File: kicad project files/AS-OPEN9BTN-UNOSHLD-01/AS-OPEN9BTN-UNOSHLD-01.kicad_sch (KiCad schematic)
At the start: 11 parts, among them J1 Conn_01x04, SW1 SW_Push, SW2 SW_Push, SW3 SW_Push, SW4 SW_Push, SW5 SW_Push, SW6 SW_Push, SW7 SW_Push, SW8 SW_Push, SW9 SW_Push

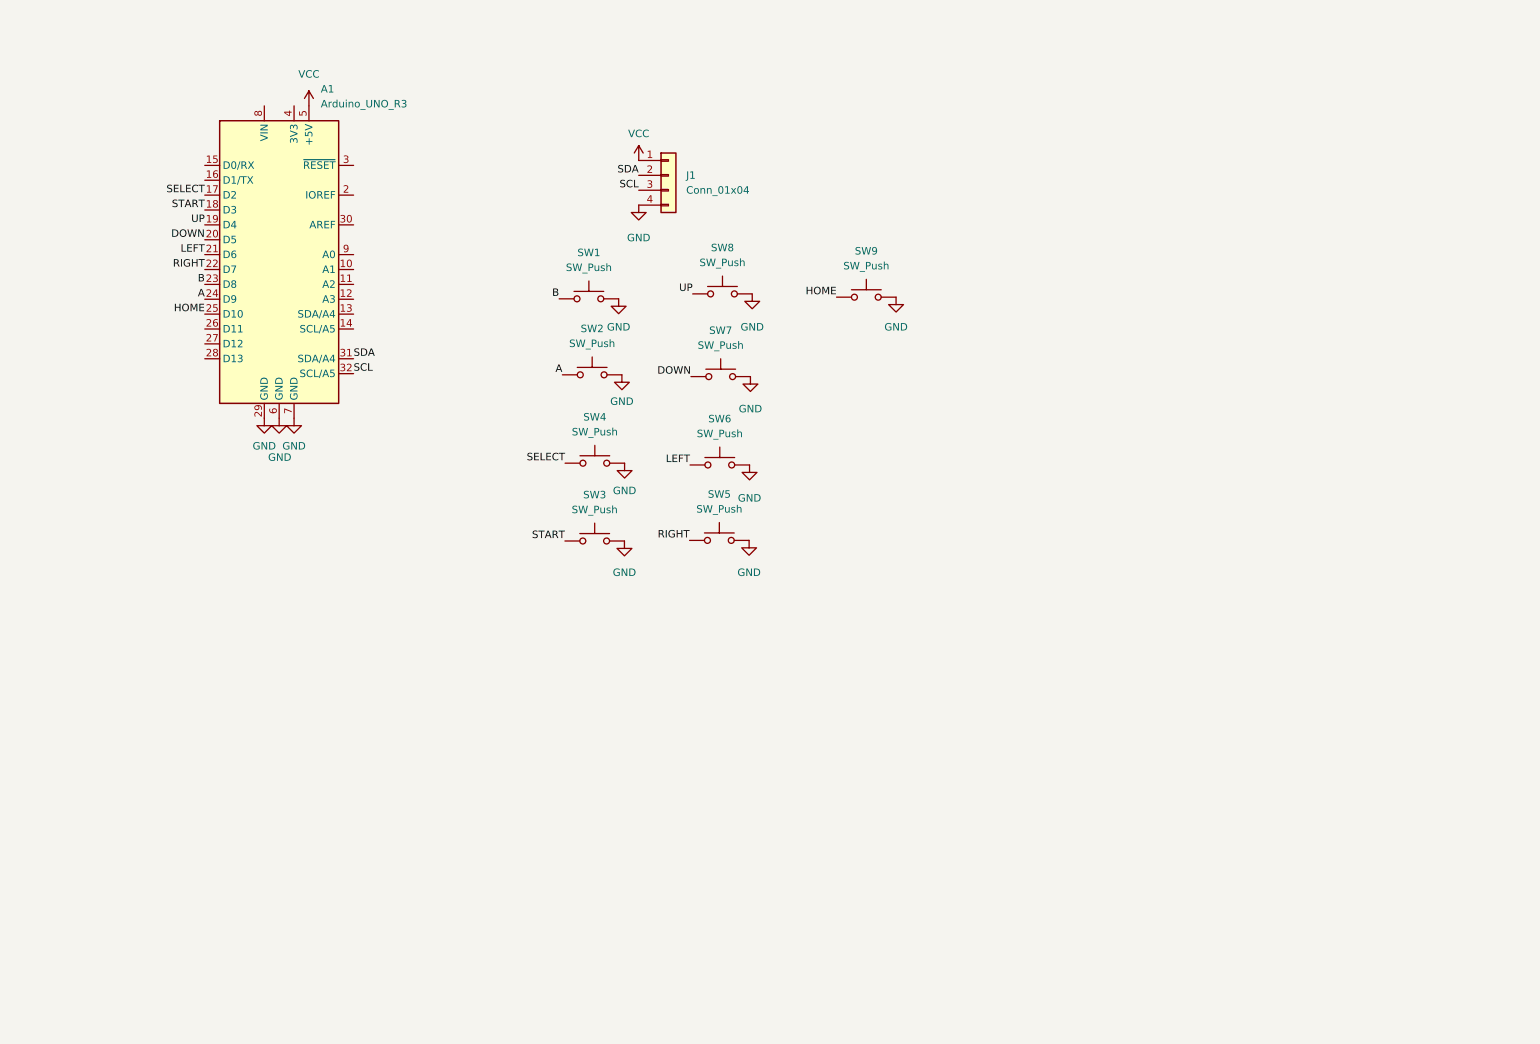
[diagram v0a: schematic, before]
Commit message: First step to voltage convertion
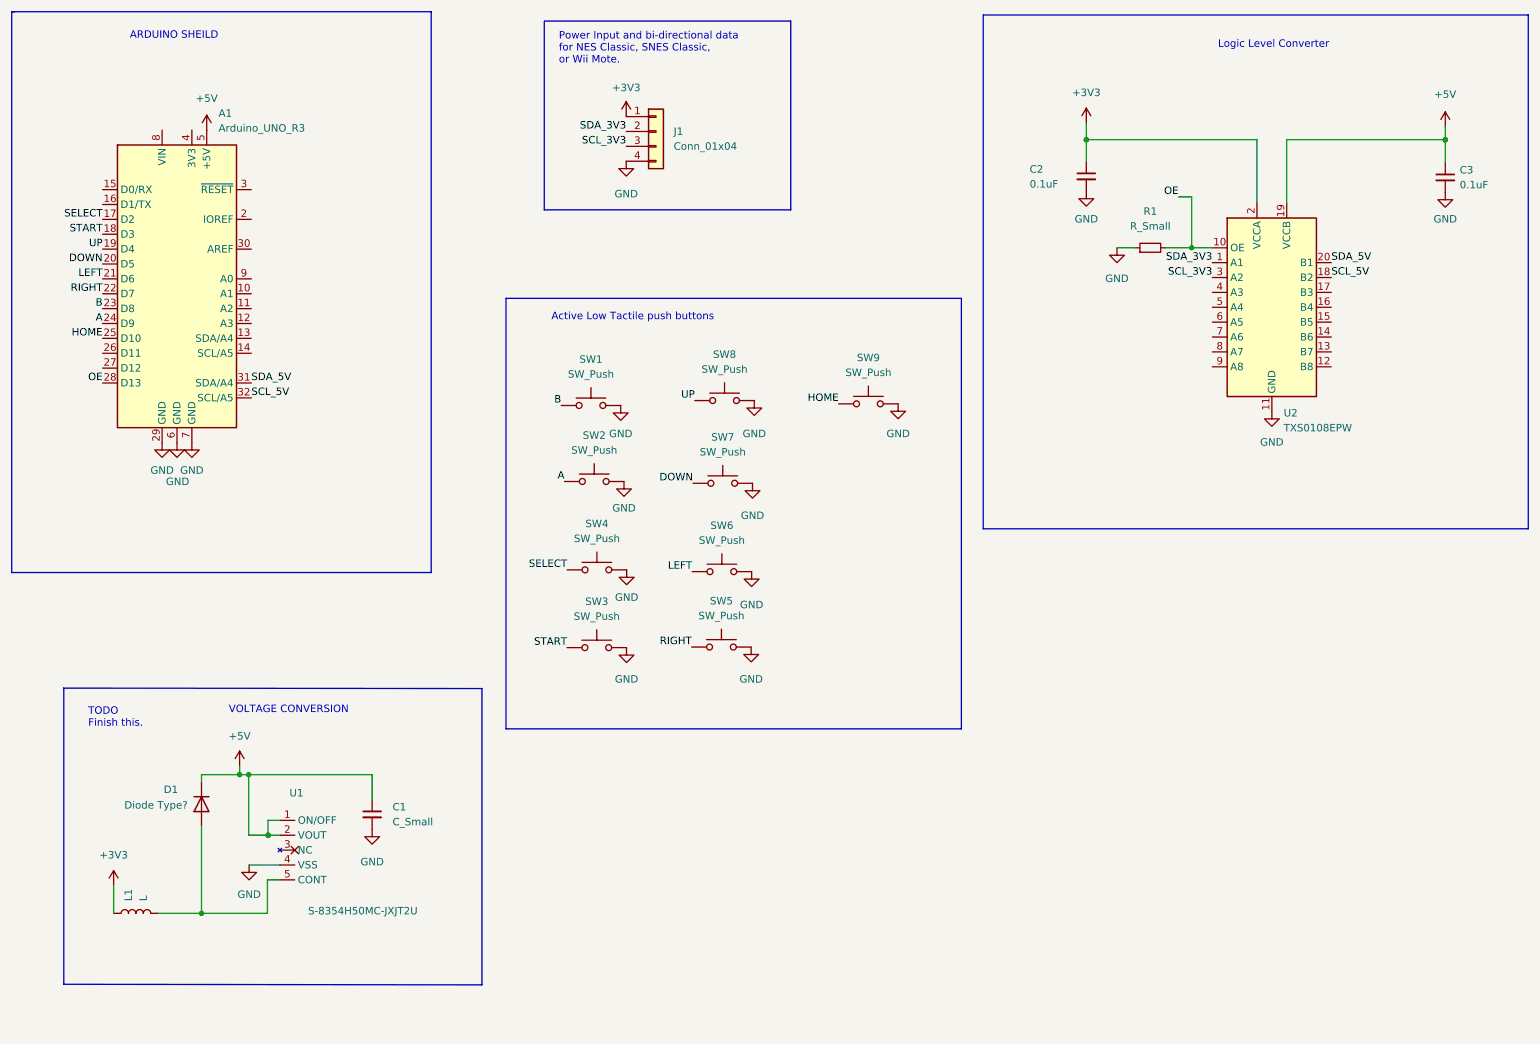
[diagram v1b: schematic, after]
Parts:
- added C1: C_Small, symbol Device:C_Small
- added C2, C3: 0.1uF, symbol Device:C_Small
- added D1: Diode Type?, Diode_THT:D_DO-41_SOD81_P10.16mm_Horizontal, symbol Diode:1N4001
- added L1: L, symbol Device:L
- added R1: R_Small, symbol Device:R_Small
- added U1: S-8354H50MC-JXJT2U, Package_TO_SOT_SMD:SOT-23-5_HandSoldering, symbol New_Library:S-8354H50MC-JXJT2U
- added U2: TXS0108EPW, Package_SO:TSSOP-20_4.4x6.5mm_P0.65mm, symbol Logic_LevelTranslator:TXS0108EPW
- J1: footprint (none) -> Connector_JST:JST_XH_B4B-XH-A_1x04_P2.50mm_Vertical
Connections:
- net GND: now also C1.2, C2.2, C3.2, R1.1, U1.4 (VSS), U2.11 (GND)
- net OE: now reaches A1.28 (D13)
- net OE: now also R1.2, U2.10 (OE)
- net SCL renamed SCL_3V3
- net SCL_3V3: now also U2.3 (A2); no longer A1.32 (SCL/A5)
- net SDA renamed SDA_3V3
- net SDA_3V3: now also U2.1 (A1); no longer A1.31 (SDA/A4)
- net VCC renamed +3V3
- net +3V3: now also C2.1, L1.1, U2.2 (VCCA); no longer A1.5 (+5V)
- new net: D1.2 (A), L1.2, U1.5 (CONT)
- new net: U1.1 (ON/OFF), U1.2 (VOUT)
- new net +5V: A1.5 (+5V), C1.1, C3.1, D1.1 (K), U2.19 (VCCB)
- new net SCL_5V: A1.32 (SCL/A5), U2.18 (B2)
- new net SDA_5V: A1.31 (SDA/A4), U2.20 (B1)
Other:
- note added: "ARDUINO SHEILD"
- note added: "Active Low Tactile push buttons"
- note added: "Logic Level Converter"
- note added: "Power Input and bi-directional data for NES Classic, SNES Classic, or Wii Mote."
- note added: "TODO Finish this."
- note added: "VOLTAGE CONVERSION"
- moved on the sheet: A1, J1, SW1, SW2, SW3, SW4, SW5, SW6, SW7, SW8, SW9

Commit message: Used smaller chip for logic level conversion
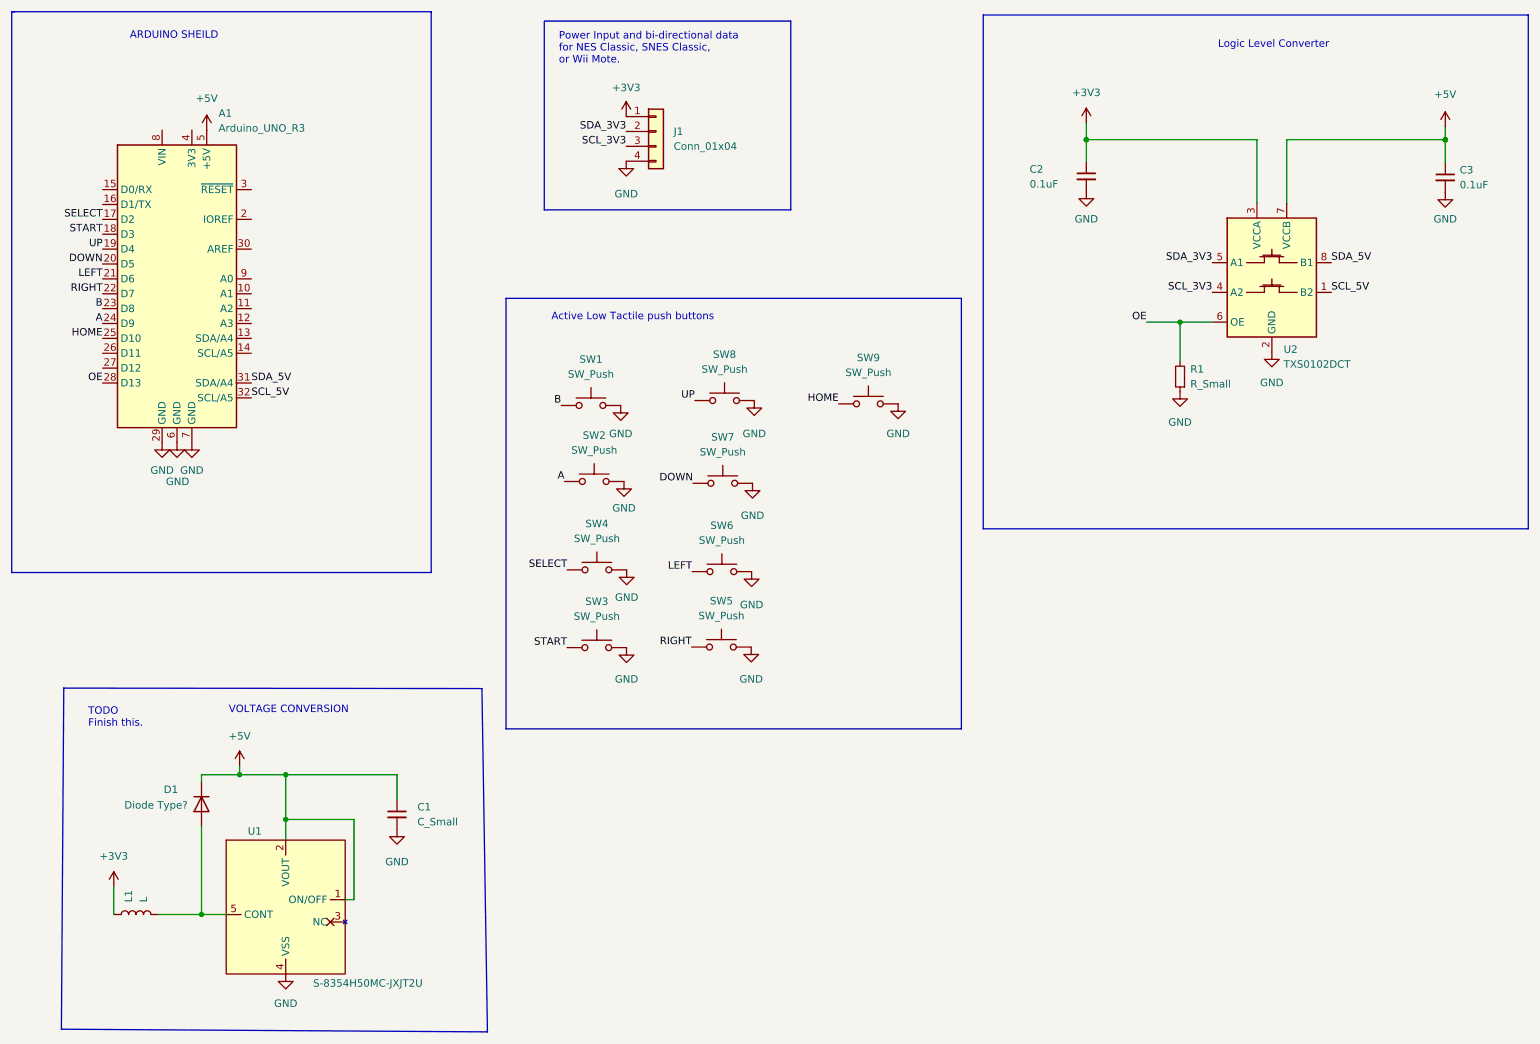
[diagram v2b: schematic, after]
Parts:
- removed U2: TXS0108EPW, Package_SO:TSSOP-20_4.4x6.5mm_P0.65mm, symbol Logic_LevelTranslator:TXS0108EPW
- added U2: TXS0102DCT, Package_SO:SSOP-8_2.95x2.8mm_P0.65mm, symbol Logic_LevelTranslator:TXS0102DCT
- U1: symbol New_Library:S-8354H50MC-JXJT2U -> New_Library:S-8354H50MC-JXJT2U_Logical
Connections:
- net +3V3: now also U2.3 (VCCA)
- net +5V: now also U1.1 (ON/OFF), U1.2 (VOUT), U2.7 (VCCB)
- net GND: now also U2.2 (GND)
- net OE: now also U2.6 (OE)
- net SCL_3V3: now also U2.4 (A2)
- net SCL_5V: now also U2.1 (B2)
- net SDA_3V3: now also U2.5 (A1)
- net SDA_5V: now also U2.8 (B1)
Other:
- moved on the sheet: C1, R1
